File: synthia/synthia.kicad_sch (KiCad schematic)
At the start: 39 parts, among them J1 MJ-63022B, J2 SJ3-35083C-TR, J3 PJ-007, Q1 IRF9540N, Q2 L78M05CV, U1 TLV272IP, U2 STM32H750ZBT6

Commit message: More updates to the Schematic, ports and solder points added for external components and were wired up
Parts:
- removed Q2: L78M05CV, Synthia_footprint_library:TO254P450X1020X1935-3P, symbol Synthia_Symbol_Library:L78M05CV
- added J4: SDS-50J, SDS-50J:CUI_SDS-50J, symbol Synthia_Symbol_Library:SDS-50J
- added TP16: Shield / Ground, TestPoint:TestPoint_Plated_Hole_D2.0mm, symbol Connector:TestPoint
- added TP17: Sink, TestPoint:TestPoint_Plated_Hole_D2.0mm, symbol Connector:TestPoint
- added TP18: Source, TestPoint:TestPoint_Plated_Hole_D2.0mm, symbol Connector:TestPoint
- added TP19: MicroUSB Pin #1, TestPoint:TestPoint_Plated_Hole_D2.0mm, symbol Connector:TestPoint
- added TP20: MicroUSB Pin #2, TestPoint:TestPoint_Plated_Hole_D2.0mm, symbol Connector:TestPoint
- added TP21: MicroUSB Pin #3, TestPoint:TestPoint_Plated_Hole_D2.0mm, symbol Connector:TestPoint
- added TP22: MicroUSB Pin #4, TestPoint:TestPoint_Plated_Hole_D2.0mm, symbol Connector:TestPoint
- added TP23: MicroUSB Pin #5, TestPoint:TestPoint_Plated_Hole_D2.0mm, symbol Connector:TestPoint
- added U3: LD1117V33, LD1117V33:TO255P1020X450X1968-3, symbol Synthia_Symbol_Library:LD1117V33
- C1: value 330nF -> 100 nF
- C2: value 100nF -> 10 uF
- R2: footprint (none) -> Synthia_footprint_library:STA_CF14_STP
- TP3: value +5V -> +3.3V
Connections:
- net +5V is gone; now on net +3.3V: C2.1, TP3.1
- net Button_Matrix/ScanCol0: now also U2.105 (PA13)
- net Button_Matrix/ScanCol1: now also U2.104 (PA12)
- net Button_Matrix/ScanCol10: now also U2.93 (PG8)
- net Button_Matrix/ScanCol11: now also U2.92 (PG7)
- net Button_Matrix/ScanCol2: now also U2.103 (PA11)
- net Button_Matrix/ScanCol3: now also U2.102 (PA10)
- net Button_Matrix/ScanCol4: now also U2.101 (PA9)
- net Button_Matrix/ScanCol5: now also U2.100 (PA8)
- net Button_Matrix/ScanCol6: now also U2.99 (PC69)
- net Button_Matrix/ScanCol7: now also U2.98 (PC8)
- net Button_Matrix/ScanCol8: now also U2.97 (PC7)
- net Button_Matrix/ScanCol9: now also U2.96 (PC6)
- net Button_Matrix/ScanRow0: now also U2.111 (PC10)
- net Button_Matrix/ScanRow1: now also U2.112 (PC11)
- net Button_Matrix/ScanRow2: now also U2.113 (PC12)
- net DAC_schematic/DAC0: now also U2.10 (PF0)
- net DAC_schematic/DAC1: now also U2.11 (PF1)
- net DAC_schematic/DAC2: now also U2.12 (PF2)
- net DAC_schematic/DAC3: now also U2.13 (PF3)
- net DAC_schematic/DAC4: now also U2.14 (PF4)
- net DAC_schematic/DAC5: now also U2.15 (PF5)
- net DAC_schematic/DAC6: now also U2.18 (PF6)
- net DAC_schematic/DAC7: now also U2.19 (PF7)
- net GND: now also TP12.1, U2.107 (VSS), U2.120 (VSS), U2.130 (VSS), U2.16 (VSS), U2.31 (VSSA), U2.38 (VSS), U2.51 (VSS), U2.61 (VSS), U2.83 (VSS), U2.94 (VSS), J4.E1 (GND), J4.E2 (GND), U3.1 (ADJ/GND)
- net at C1.1, D1.1 (K), Q1.3 (S): now also U3.3 (VIN)
- net at TP11.1: now also U2.142 (PE1)
- net +3.3V: now reaches U2.17 (VDD)
- net +3.3V: now also TP10.1, U2.108 (VDD), U2.121 (VDD), U2.131 (VDD), U2.144 (VDD), U2.30 (VDD), U2.33 (VDDA), U2.39 (VDD), U2.52 (VDD), U2.6 (VBAT), U2.62 (VDD), U2.72 (VDD), U2.84 (VDD), U3.2 (VOUT)
- new net: J4.2, TP16.1
- new net: J4.4, TP17.1
- new net: J4.5, TP18.1
- no-connect marks 0 -> 5
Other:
- note added: "MIDI Component to implement Later"
- moved on the sheet: C2, TP10, TP11, TP12, TP3, U2A, U2B

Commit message: More updates to Schematic, added latching switch as a symbol and footprint
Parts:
- removed TP22: MicroUSB Pin #4, TestPoint:TestPoint_Plated_Hole_D2.0mm, symbol Connector:TestPoint
- removed TP23: MicroUSB Pin #5, TestPoint:TestPoint_Plated_Hole_D2.0mm, symbol Connector:TestPoint
- added R51, R52, R53, R54, R55, R56, R57, R58, R59, R60, R61, R62, R63, R64, R65, R66, R67, R68, R69, R70, R71, R72, R73, R74, R75, R76, R77, R78: 100k, Synthia_footprint_library:STA_CF14_STP, symbol Device:R_US
- added S37, S38, S39, S40, S41, S43, S44, S45, S46, S47: TL1105BF160Q, Synthia_footprint_library:SW_TL1105BF160Q, symbol Synthia_Symbol_Library:TL1105BF160Q
- added S42: RESET, Synthia_footprint_library:SW_TL1105BF160Q, symbol Synthia_Symbol_Library:TL1105BF160Q
- C1, C2, C3: footprint (none) -> Capacitor_THT:CP_Radial_Tantal_D5.0mm_P5.00mm
- J1: footprint MJ-63022B:CUI_MJ-63022B -> Synthia_footprint_library:CUI_MJ-63022B
- J2: footprint SJ3-35083C-TR:SAMESKY_SJ3-35083C-TR -> Synthia_footprint_library:SAMESKY_SJ3-35083C-TR
- J3: footprint PJ-007:SAMESKY_PJ-007 -> Synthia_footprint_library:SAMESKY_PJ-007
- J4: footprint SDS-50J:CUI_SDS-50J -> Synthia_footprint_library:CUI_SDS-50J
- R50: footprint POT_P120PK-x25_TTE -> Synthia_footprint_library:POT_P120PK-x25_TTE
- TP19: value MicroUSB Pin #1 -> MicroUSB D- Pin
- TP20: value MicroUSB Pin #2 -> MicroUSB D+ Pin
- TP21: value MicroUSB Pin #3 -> MicroUSB GND
- U1: footprint Synthia_footprint_library:POT_P120PK-x25_TTE -> Synthia_footprint_library:DIP794W45P254L959H508Q8
- U2: footprint LQFP144_STM -> Synthia_footprint_library:LQFP144_STM
- U3: footprint LD1117V33:TO255P1020X450X1968-3 -> Synthia_footprint_library:TO255P1020X450X1968-3
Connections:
- net +3.3V: now also U2.138 (BOOT0), U2.143 (PDR_ON), U2.32 (VREF+), U2.95 (VDD33USB), S37.2, S38.2, S39.2, S40.2, S41.2, S43.2, S44.2, S45.2, S46.2, S47.2
- net Button_Matrix/ScanCol0: no longer U2.105 (PA13)
- net Button_Matrix/ScanCol1: no longer U2.104 (PA12)
- net Button_Matrix/ScanCol10: no longer U2.93 (PG8)
- net Button_Matrix/ScanCol11: no longer U2.92 (PG7)
- net Button_Matrix/ScanCol2: no longer U2.103 (PA11)
- net Button_Matrix/ScanCol3: no longer U2.102 (PA10)
- net Button_Matrix/ScanCol4: no longer U2.101 (PA9)
- net Button_Matrix/ScanCol5: no longer U2.100 (PA8)
- net Button_Matrix/ScanCol6: no longer U2.99 (PC69)
- net Button_Matrix/ScanCol7: no longer U2.98 (PC8)
- net Button_Matrix/ScanCol8: no longer U2.97 (PC7)
- net Button_Matrix/ScanCol9: no longer U2.96 (PC6)
- net Button_Matrix/ScanRow0: no longer U2.111 (PC10)
- net Button_Matrix/ScanRow1: no longer U2.112 (PC11)
- net Button_Matrix/ScanRow2: no longer U2.113 (PC12)
- net GND: now also TP21.1, S42.1
- net at TP20.1: now also U2.104 (PA12)
- net at TP19.1: now also U2.103 (PA11)
- net at U2.25 (NRST): now also S42.3
- new net: R58.2, R61.2, R62.1
- new net: R56.2, R62.2, R63.1
- new net: R53.1, S38.4
- new net: R53.2, R54.1
- new net: R66.2, R67.1
- new net: R67.2, R69.2, R70.1
- new net: R55.1, S39.4
- new net: R55.2, R56.1
- new net: R71.1, S45.4
- new net: R71.2, R72.1
- new net: R77.1, S47.4
- new net: R77.2, R78.1
- new net: R74.2, R75.1
- new net: R73.2, R75.2, R76.1
- new net: R65.2, R66.1
- new net: R74.1, S46.4
- new net: R59.1, S41.4
- new net: R59.2, R60.1
- new net: R60.2, R61.1
- new net: R57.1, S40.4
- new net: R51.2, R52.1
- new net: R52.2, R64.2
- new net: R70.2, R72.2, R73.1
- new net: R68.2, R69.1
- new net: R51.1, S37.4
- new net: R68.1, S44.4
- new net: R57.2, R58.1
- new net: R54.2, R63.2, R64.1
- new net: R65.1, S43.4
- new net: R76.2, R78.2
- no-connect marks 5 -> 26
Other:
- moved on the sheet: TP14

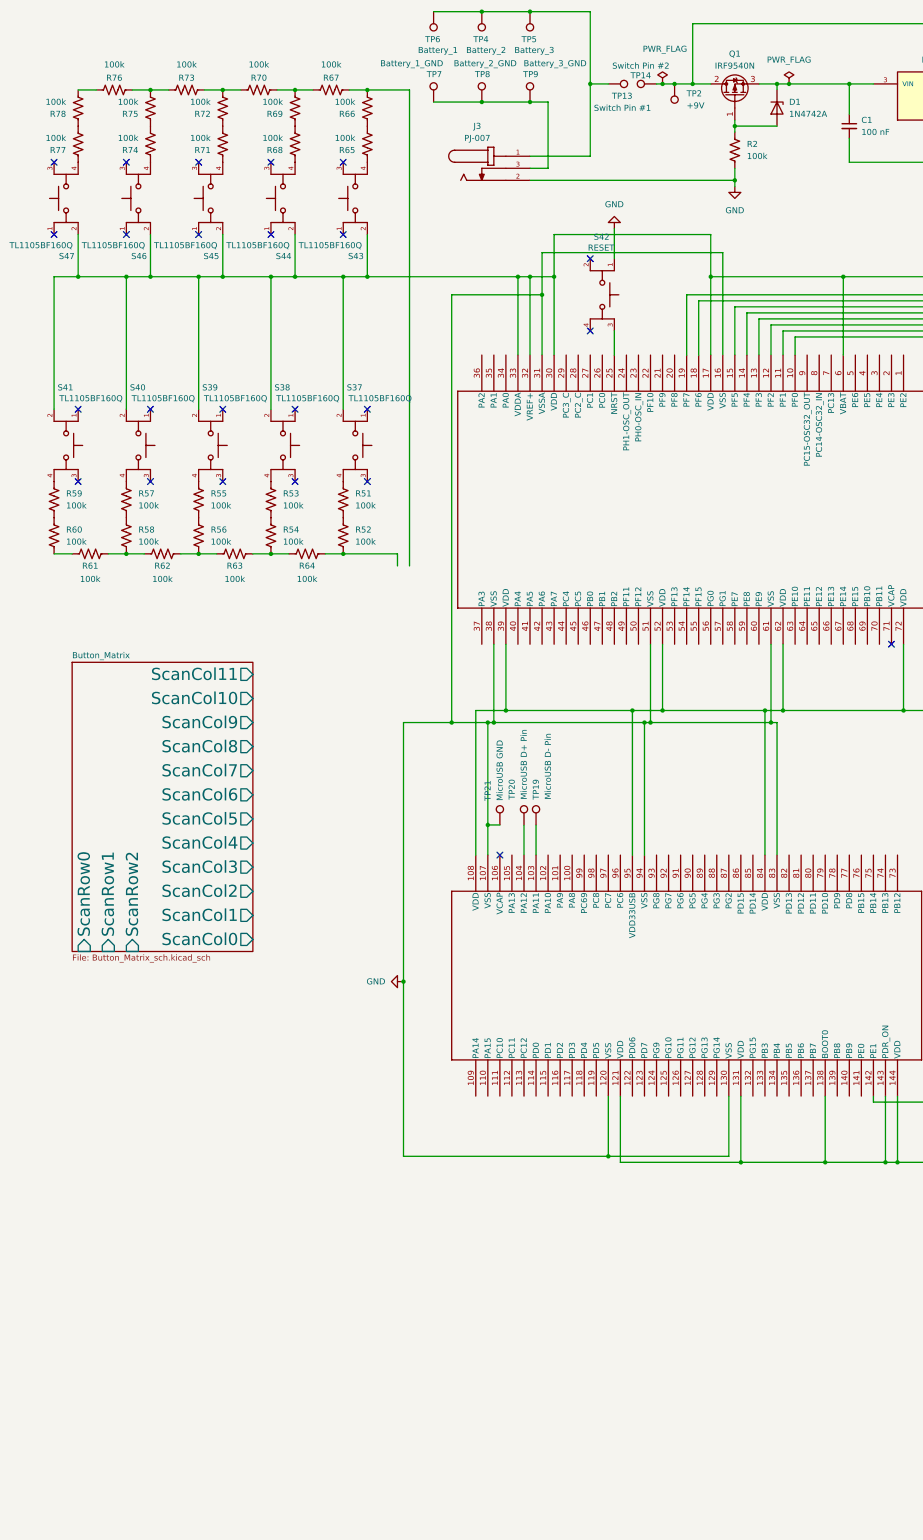
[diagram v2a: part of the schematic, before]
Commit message: More changes made during Jank. Made a symbol and footprint for the latching switch
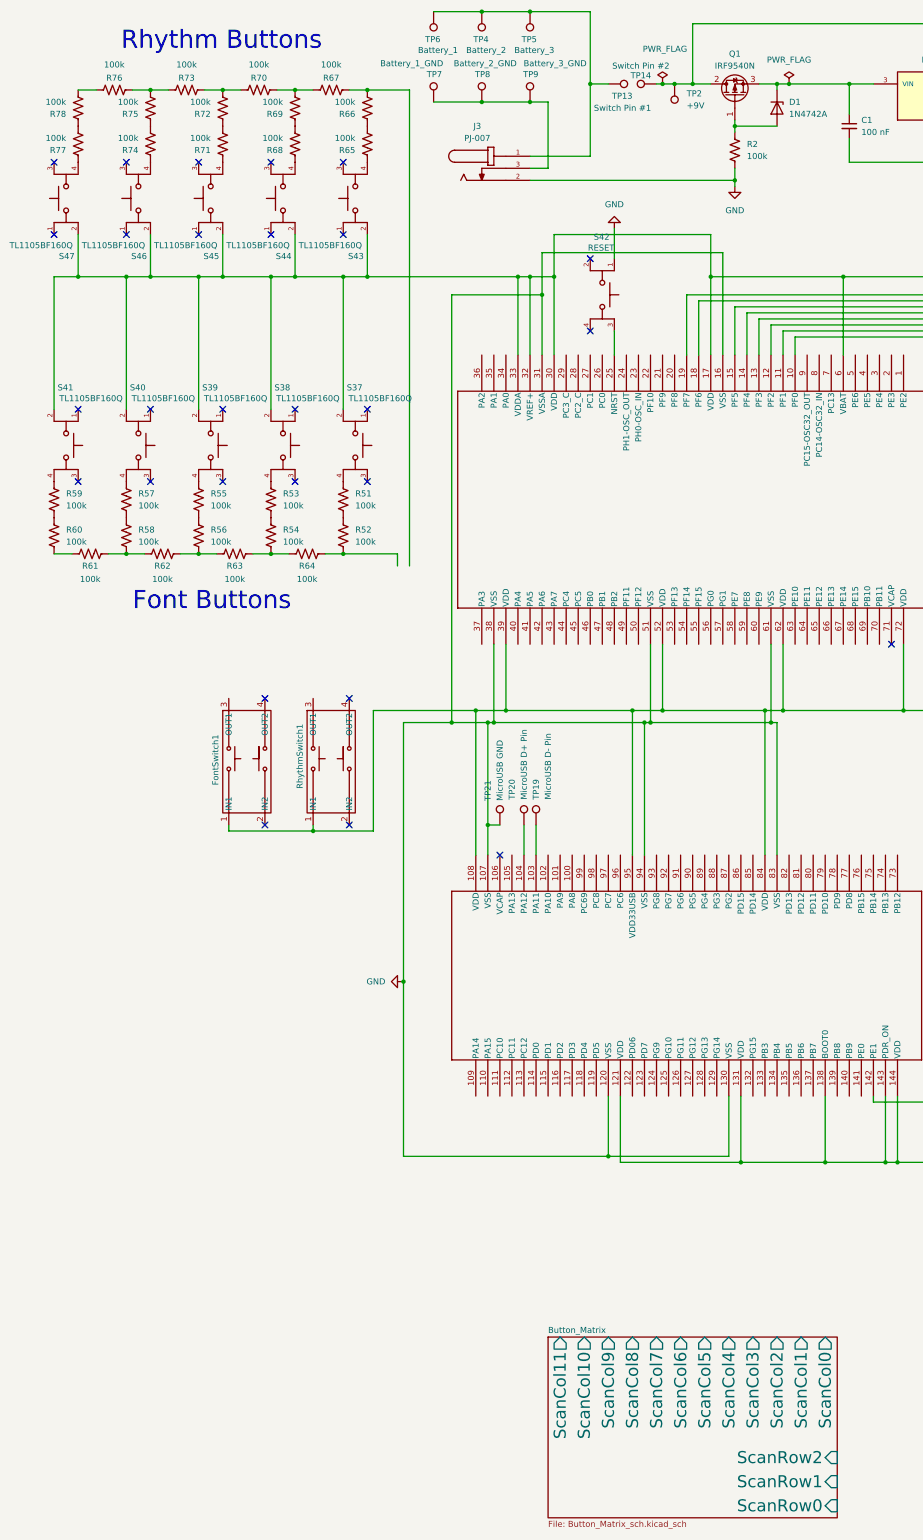
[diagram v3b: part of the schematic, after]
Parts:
- added FontSwitch1, RhythmSwitch1: (no value), Synthia_footprint_library:Latching Switch, symbol Synthia_Symbol_Library:Latching_switch
- R1, R12, R41, R42, R43, R44, R45, R46, R47, R48, R49: footprint (none) -> Synthia_footprint_library:STA_CF14_STP
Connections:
- net +3.3V: now also FontSwitch1.1 (IN1), RhythmSwitch1.1 (IN1)
- no-connect marks 26 -> 30
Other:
- note added: "Font Buttons"
- note added: "Rhythm Buttons"

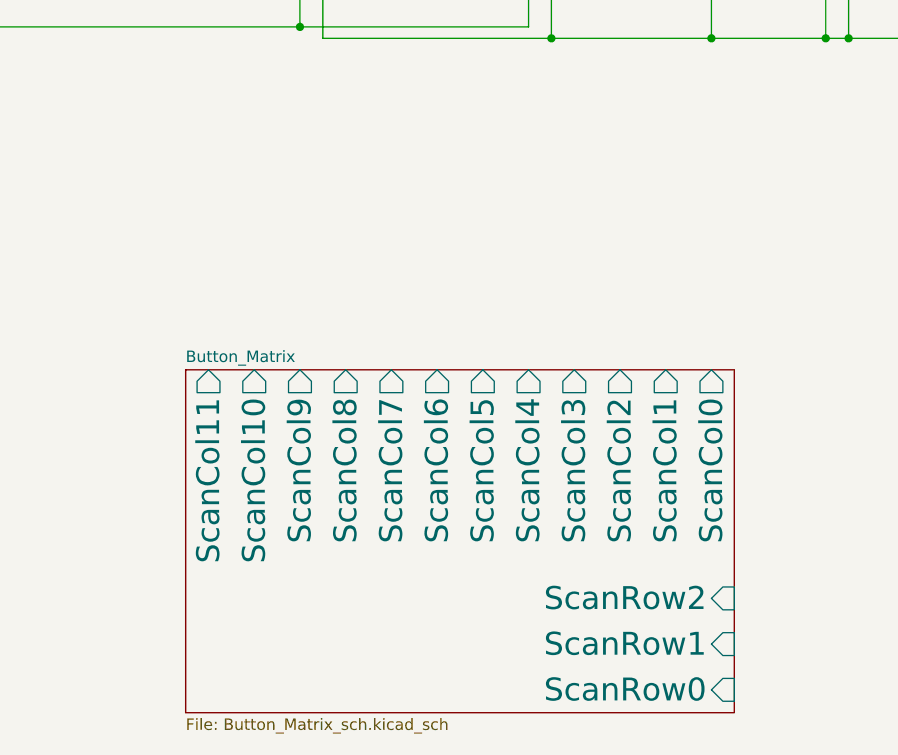
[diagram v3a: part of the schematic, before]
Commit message: did some pcb work, initial wiring complete
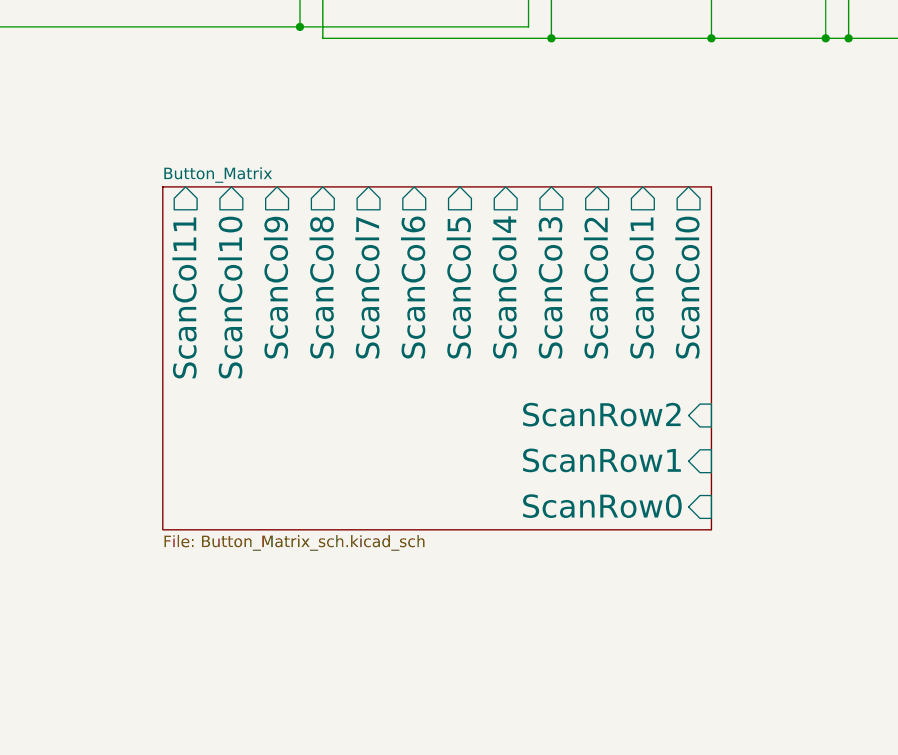
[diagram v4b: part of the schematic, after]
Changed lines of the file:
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@@
 	)
 	(sheet
-		(at 120.65 307.34)
+		(at 118.11 287.02)
 		(size 60.96 38.1)
 		(exclude_from_sim no)
@@
 		)
 		(property "Sheetname" "Button_Matrix"
-			(at 120.65 306.6284 0)
+			(at 118.11 286.3084 0)
 			(show_name no)
 			(do_not_autoplace no)
@@
 		)
 		(property "Sheetfile" "Button_Matrix_sch.kicad_sch"
-			(at 120.65 346.0246 0)
+			(at 118.11 325.7046 0)
 			(show_name no)
 			(do_not_autoplace no)
@@
 		)
 		(pin "ScanCol0" output
-			(at 179.07 307.34 90)
+			(at 176.53 287.02 90)
 			(effects
 				(font
@@
 		)
 		(pin "ScanCol1" output
-			(at 173.99 307.34 90)
+			(at 171.45 287.02 90)
 			(effects
 				(font
@@
 		)
 		(pin "ScanCol2" output
-			(at 168.91 307.34 90)
+			(at 166.37 287.02 90)
 			(effects
 				(font
@@
 		)
 		(pin "ScanCol3" output
-			(at 163.83 307.34 90)
+			(at 161.29 287.02 90)
 			(effects
 				(font
@@
 		)
 		(pin "ScanCol4" output
-			(at 158.75 307.34 90)
+			(at 156.21 287.02 90)
 			(effects
 				(font
@@
 		)
 		(pin "ScanCol5" output
-			(at 153.67 307.34 90)
+			(at 151.13 287.02 90)
 			(effects
 				(font
@@
 		)
 		(pin "ScanCol6" output
-			(at 148.59 307.34 90)
+			(at 146.05 287.02 90)
 			(effects
 				(font
@@
 		)
 		(pin "ScanCol7" output
-			(at 143.51 307.34 90)
+			(at 140.97 287.02 90)
 			(effects
 				(font
@@
 		)
 		(pin "ScanCol8" output
-			(at 138.43 307.34 90)
+			(at 135.89 287.02 90)
 			(effects
 				(font
@@
 		)
 		(pin "ScanCol9" output
-			(at 133.35 307.34 90)
+			(at 130.81 287.02 90)
 			(effects
 				(font
@@
 		)
 		(pin "ScanCol10" output
-			(at 128.27 307.34 90)
+			(at 125.73 287.02 90)
 			(effects
 				(font
@@
 		)
 		(pin "ScanCol11" output
-			(at 123.19 307.34 90)
+			(at 120.65 287.02 90)
 			(effects
 				(font
@@
 		)
 		(pin "ScanRow0" input
-			(at 181.61 342.9 0)
+			(at 179.07 322.58 0)
 			(effects
 				(font
@@
 		)
 		(pin "ScanRow1" input
-			(at 181.61 337.82 0)
+			(at 179.07 317.5 0)
 			(effects
 				(font
@@
 		)
 		(pin "ScanRow2" input
-			(at 181.61 332.74 0)
+			(at 179.07 312.42 0)
 			(effects
 				(font
